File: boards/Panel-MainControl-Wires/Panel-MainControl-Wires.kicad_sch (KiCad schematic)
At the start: 4 parts, among them J1 Volume

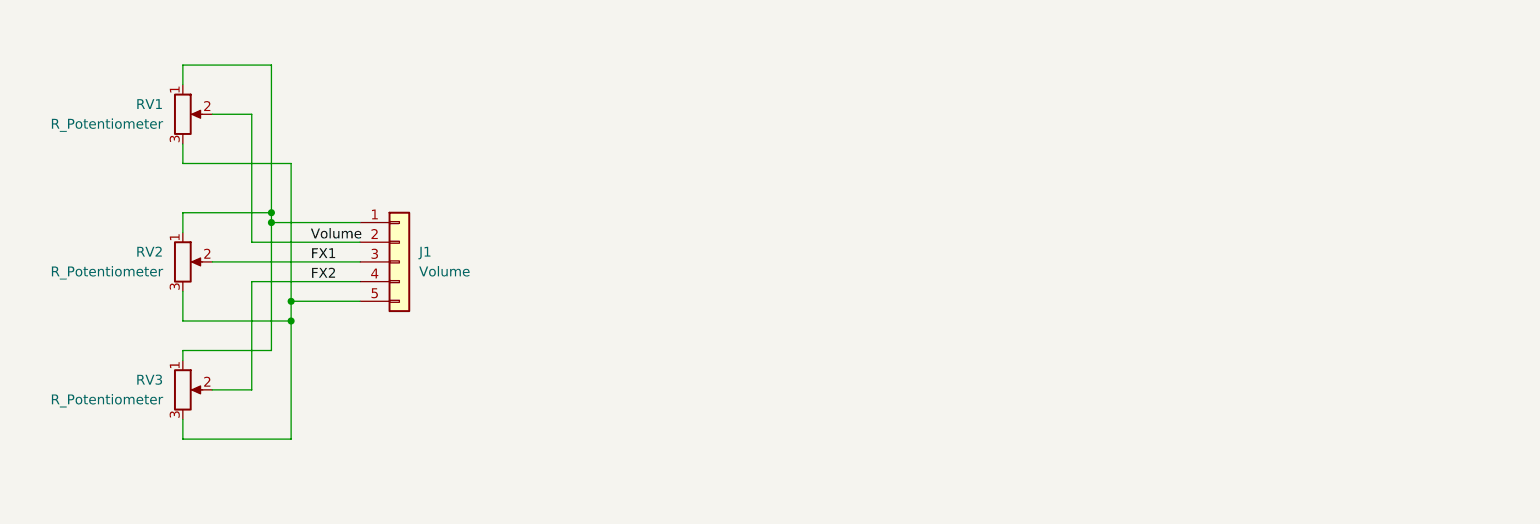
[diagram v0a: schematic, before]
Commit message: Added panel design files and panel schematics
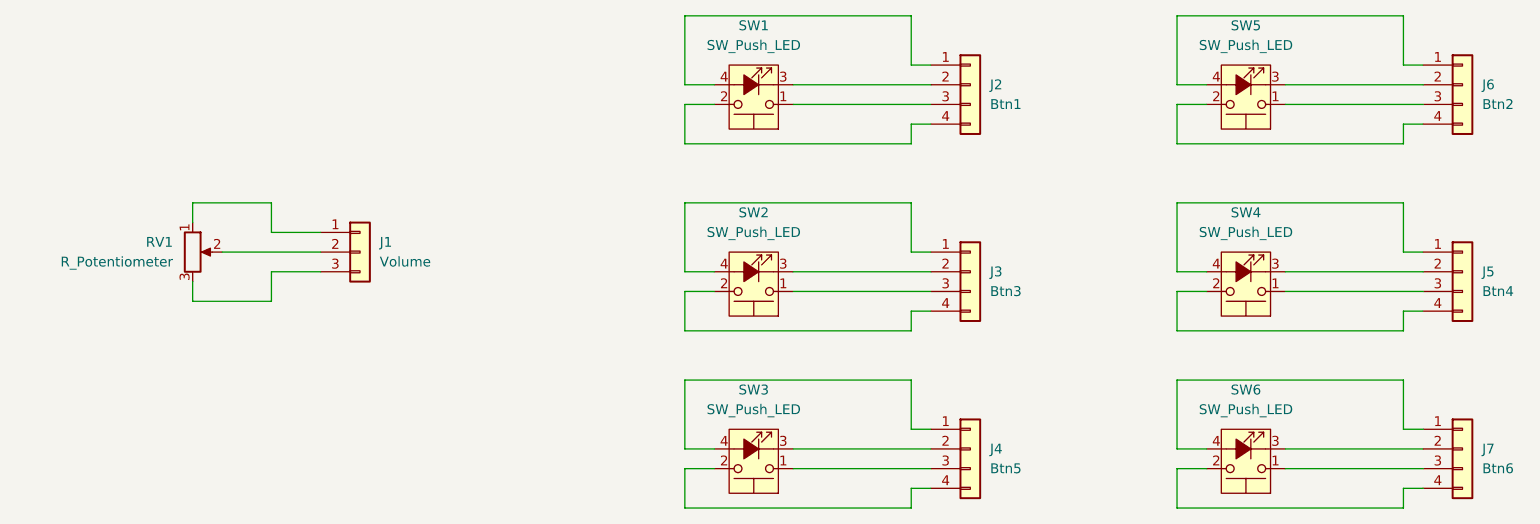
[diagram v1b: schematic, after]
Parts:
- removed J1: Volume, symbol Connector_Generic:Conn_01x05
- removed RV2, RV3: R_Potentiometer, symbol Device:R_Potentiometer
- added J1: Volume, symbol Connector_Generic:Conn_01x03
- added J2: Btn1, symbol Connector_Generic:Conn_01x04
- added J3: Btn3, symbol Connector_Generic:Conn_01x04
- added J4: Btn5, symbol Connector_Generic:Conn_01x04
- added J5: Btn4, symbol Connector_Generic:Conn_01x04
- added J6: Btn2, symbol Connector_Generic:Conn_01x04
- added J7: Btn6, symbol Connector_Generic:Conn_01x04
- added SW1, SW2, SW3, SW4, SW5, SW6: SW_Push_LED, symbol Switch:SW_Push_LED
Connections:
- net at RV1.1: now also J1.1 (Pin_1)
- net at RV1.3: now also J1.3 (Pin_3)
- net Volume: no longer names the net of RV1.2
- net Volume: now also J1.2 (Pin_2)
- new net: J3.3 (Pin_3), SW2.1
- new net: J3.4 (Pin_4), SW2.2
- new net: J3.2 (Pin_2), SW2.3 (K)
- new net: J3.1 (Pin_1), SW2.4 (A)
- new net: J6.3 (Pin_3), SW5.1
- new net: J6.4 (Pin_4), SW5.2
- new net: J6.2 (Pin_2), SW5.3 (K)
- new net: J6.1 (Pin_1), SW5.4 (A)
- new net: J2.3 (Pin_3), SW1.1
- new net: J2.4 (Pin_4), SW1.2
- new net: J2.2 (Pin_2), SW1.3 (K)
- new net: J2.1 (Pin_1), SW1.4 (A)
- new net: J5.1 (Pin_1), SW4.4 (A)
- new net: J5.2 (Pin_2), SW4.3 (K)
- new net: J5.3 (Pin_3), SW4.1
- new net: J5.4 (Pin_4), SW4.2
- new net: J4.3 (Pin_3), SW3.1
- new net: J4.4 (Pin_4), SW3.2
- new net: J4.2 (Pin_2), SW3.3 (K)
- new net: J4.1 (Pin_1), SW3.4 (A)
- new net: J7.1 (Pin_1), SW6.4 (A)
- new net: J7.2 (Pin_2), SW6.3 (K)
- new net: J7.3 (Pin_3), SW6.1
- new net: J7.4 (Pin_4), SW6.2
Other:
- moved on the sheet: RV1
